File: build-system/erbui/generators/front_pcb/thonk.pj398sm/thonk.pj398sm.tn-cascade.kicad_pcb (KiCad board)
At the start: 2 copper layers, 4 parts, among them J1 IN

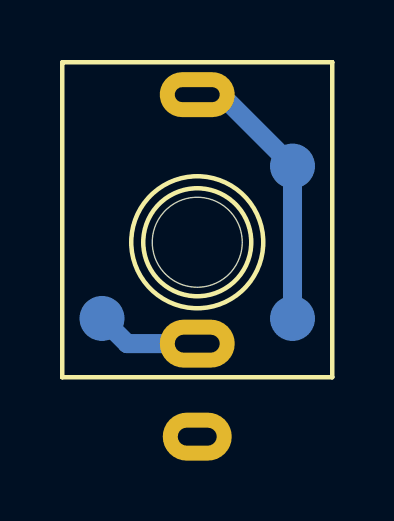
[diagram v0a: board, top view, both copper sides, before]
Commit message: Update thonk connector for cascade parts
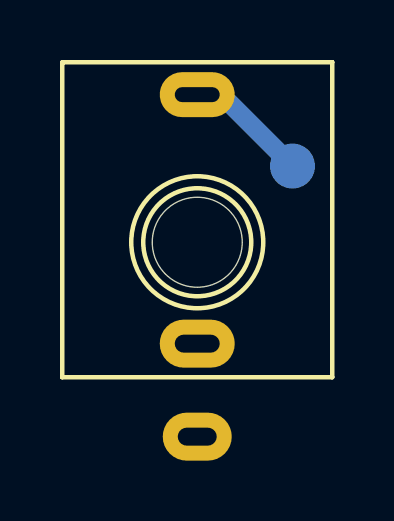
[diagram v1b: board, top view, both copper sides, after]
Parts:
- removed TP2, TP3: TestPoint, TestPoint:TestPoint_Pad_D1.5mm
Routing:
- net Net-(J1-PadT): track 9.24 -> 4.16 mm
- net Net-(J1-PadTN): track 3.52 -> 0.00 mm
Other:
- board text removed: "DI"
- board text removed: "DO"
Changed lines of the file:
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@@
   (general
     (thickness 1.6)
-    (drawings 3)
-    (tracks 5)
+    (drawings 1)
+    (tracks 2)
     (zones 0)
-    (modules 4)
+    (modules 2)
     (nets 4)
   )
@@
   )
   (setup
-    (last_trace_width 0.635)
+    (last_trace_width 0.1524)
     (user_trace_width 0.1524)
     (user_trace_width 0.254)
@@
       (effects (font (size 1 1) (thickness 0.15)))
     )
+    (fp_circle (center 0 0) (end 2.2 0) (layer F.SilkS) (width 0.15))
+    (fp_line (start -4.5 4.5) (end 4.5 4.5) (layer F.SilkS) (width 0.15))
+    (fp_line (start 4.5 -6) (end 4.5 4.5) (layer F.SilkS) (width 0.15))
+    (fp_line (start -4.5 -6) (end -4.5 4.5) (layer F.SilkS) (width 0.15))
+    (fp_line (start -4.5 -6) (end 4.5 -6) (layer F.SilkS) (width 0.15))
     (fp_circle (center 0 0) (end 1.8 0) (layer F.SilkS) (width 0.15))
-    (fp_line (start -4.5 -6) (end 4.5 -6) (layer F.SilkS) (width 0.15))
-    (fp_line (start -4.5 -6) (end -4.5 4.5) (layer F.SilkS) (width 0.15))
-    (fp_line (start 4.5 -6) (end 4.5 4.5) (layer F.SilkS) (width 0.15))
-    (fp_line (start -4.5 4.5) (end 4.5 4.5) (layer F.SilkS) (width 0.15))
-    (fp_circle (center 0 0) (end 2.2 0) (layer F.SilkS) (width 0.15))
     (pad "" np_thru_hole circle (at 0 0) (size 3 3) (drill 3) (layers *.Cu *.Mask))
     (pad T thru_hole oval (at 0 -4.92) (size 2.5 1.5) (drill oval 1.5 0.5) (layers *.Cu *.Mask)
@@
       (effects (font (size 1 1) (thickness 0.15)) (justify mirror))
     )
+    (fp_circle (center 0 0) (end 1.25 0) (layer B.CrtYd) (width 0.05))
     (fp_circle (center 0 0) (end 0 -0.95) (layer B.SilkS) (width 0.12))
-    (fp_circle (center 0 0) (end 1.25 0) (layer B.CrtYd) (width 0.05))
     (fp_text user %R (at 0 1.65) (layer B.Fab)
       (effects (font (size 1 1) (thickness 0.15)) (justify mirror))
@@
       (net 2 "Net-(J1-PadT)"))
   )
-  (module TestPoint:TestPoint_Pad_D1.5mm (layer B.Cu)
-    (at -3.175 2.54)
-    (descr "SMD pad as test Point, diameter 1.5mm")
-    (tags "test point SMD pad")
-    (attr virtual)
-    (fp_text reference TP3 (at 0 1.648) (layer B.SilkS) hide
-      (effects (font (size 1 1) (thickness 0.15)) (justify mirror))
-    )
-    (fp_text value TestPoint (at 0 -1.75) (layer B.Fab)
-      (effects (font (size 1 1) (thickness 0.15)) (justify mirror))
-    )
-    (fp_circle (center 0 0) (end 1.25 0) (layer B.CrtYd) (width 0.05))
-    (fp_circle (center 0 0) (end 0 -0.95) (layer B.SilkS) (width 0.12))
-    (fp_text user %R (at 0 1.65) (layer B.Fab)
-      (effects (font (size 1 1) (thickness 0.15)) (justify mirror))
-    )
-    (pad 1 smd circle (at 0 0) (size 1.5 1.5) (layers B.Cu B.Mask)
-      (net 1 "Net-(J1-PadTN)"))
-  )
-  (module TestPoint:TestPoint_Pad_D1.5mm (layer B.Cu)
-    (at 3.175 2.54)
-    (descr "SMD pad as test Point, diameter 1.5mm")
-    (tags "test point SMD pad")
-    (attr virtual)
-    (fp_text reference TP2 (at 0 1.648) (layer B.SilkS) hide
-      (effects (font (size 1 1) (thickness 0.15)) (justify mirror))
-    )
-    (fp_text value TestPoint (at 0 -1.75) (layer B.Fab)
-      (effects (font (size 1 1) (thickness 0.15)) (justify mirror))
-    )
-    (fp_circle (center 0 0) (end 0 -0.95) (layer B.SilkS) (width 0.12))
-    (fp_circle (center 0 0) (end 1.25 0) (layer B.CrtYd) (width 0.05))
-    (fp_text user %R (at 0 1.65) (layer B.Fab)
-      (effects (font (size 1 1) (thickness 0.15)) (justify mirror))
-    )
-    (pad 1 smd circle (at 0 0) (size 1.5 1.5) (layers B.Cu B.Mask)
-      (net 2 "Net-(J1-PadT)"))
-  )
-  (gr_text DO (at 3.175 0.635) (layer B.SilkS)
-    (effects (font (size 1 1) (thickness 0.15)) (justify mirror))
-  )
-  (gr_text DI (at -3.175 0.635) (layer B.SilkS)
-    (effects (font (size 1 1) (thickness 0.15)) (justify mirror))
-  )
   (gr_text pin (at 3.175 -4.445) (layer B.SilkS)
     (effects (font (size 1 1) (thickness 0.15)) (justify mirror))
   )
-  (segment (start -2.335 3.38) (end -3.175 2.54) (width 0.635) (layer B.Cu) (net 1))
-  (segment (start 0 3.38) (end -2.335 3.38) (width 0.635) (layer B.Cu) (net 1))
   (segment (start 0.795 -4.92) (end 3.175 -2.54) (width 0.635) (layer B.Cu) (net 2))
   (segment (start 0 -4.92) (end 0.795 -4.92) (width 0.635) (layer B.Cu) (net 2))
-  (segment (start 3.175 -2.54) (end 3.175 2.54) (width 0.635) (layer B.Cu) (net 2))
 )

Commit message: Optimize thonkiconn by reducing center hole and tightening pads
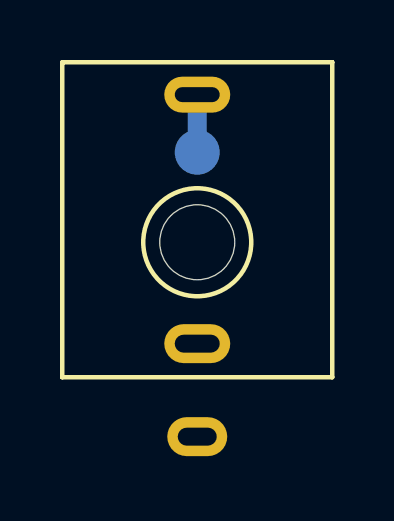
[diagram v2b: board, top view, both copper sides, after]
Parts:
- moved TP1 3.21 mm to (0.00, -3.00)
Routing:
- net Net-(J1-PadT): track 4.16 -> 1.92 mm
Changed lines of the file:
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@@
     (thickness 1.6)
     (drawings 1)
-    (tracks 2)
+    (tracks 1)
     (zones 0)
     (modules 2)
@@
     (mod_text_size 1 1)
     (mod_text_width 0.15)
-    (pad_size 2.3 1.6)
+    (pad_size 2 1.3)
     (pad_drill 1.3)
     (pad_to_mask_clearance 0.2)
@@
       (effects (font (size 1 1) (thickness 0.15)))
     )
-    (fp_circle (center 0 0) (end 2.2 0) (layer F.SilkS) (width 0.15))
     (fp_line (start -4.5 4.5) (end 4.5 4.5) (layer F.SilkS) (width 0.15))
     (fp_line (start 4.5 -6) (end 4.5 4.5) (layer F.SilkS) (width 0.15))
@@
     (fp_line (start -4.5 -6) (end 4.5 -6) (layer F.SilkS) (width 0.15))
     (fp_circle (center 0 0) (end 1.8 0) (layer F.SilkS) (width 0.15))
-    (pad "" np_thru_hole circle (at 0 0) (size 3 3) (drill 3) (layers *.Cu *.Mask))
-    (pad T thru_hole oval (at 0 -4.92) (size 2.5 1.5) (drill oval 1.5 0.5) (layers *.Cu *.Mask)
+    (pad "" np_thru_hole circle (at 0 0) (size 2.5 2.5) (drill 2.5) (layers *.Cu *.Mask))
+    (pad T thru_hole oval (at 0 -4.92) (size 2.2 1.2) (drill oval 1.5 0.5) (layers *.Cu *.Mask)
       (net 2 "Net-(J1-PadT)"))
-    (pad TN thru_hole oval (at 0 3.38) (size 2.5 1.6) (drill oval 1.5 0.6) (layers *.Cu *.Mask)
+    (pad TN thru_hole oval (at 0 3.38) (size 2.2 1.3) (drill oval 1.5 0.6) (layers *.Cu *.Mask)
       (net 1 "Net-(J1-PadTN)"))
-    (pad S thru_hole oval (at 0 6.48) (size 2.3 1.6) (drill oval 1.3 0.6) (layers *.Cu *.Mask)
+    (pad S thru_hole oval (at 0 6.48) (size 2 1.3) (drill oval 1.3 0.6) (layers *.Cu *.Mask)
       (net 3 GND))
   )
   (module TestPoint:TestPoint_Pad_D1.5mm (layer B.Cu)
-    (at 3.175 -2.54)
+    (at 0 -3)
     (descr "SMD pad as test Point, diameter 1.5mm")
     (tags "test point SMD pad")
@@
       (net 2 "Net-(J1-PadT)"))
   )
-  (gr_text pin (at 3.175 -4.445) (layer B.SilkS)
-    (effects (font (size 1 1) (thickness 0.15)) (justify mirror))
+  (gr_text pin (at -0.95 -3) (layer B.SilkS)
+    (effects (font (size 1 1) (thickness 0.15)) (justify left mirror))
   )
-  (segment (start 0.795 -4.92) (end 3.175 -2.54) (width 0.635) (layer B.Cu) (net 2))
-  (segment (start 0 -4.92) (end 0.795 -4.92) (width 0.635) (layer B.Cu) (net 2))
+  (segment (start 0 -4.92) (end 0 -3) (width 0.635) (layer B.Cu) (net 2))
 )

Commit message: Assign predictable pin names to controls
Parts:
- renumbered TP1 to Pin0, J1 to ZZ1
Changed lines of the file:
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@@
   )
   (net 0 "")
-  (net 1 "Net-(J1-PadTN)")
-  (net 2 "Net-(J1-PadT)")
-  (net 3 GND)
+  (net 1 GND)
+  (net 2 "Net-(Pin0-Pad1)")
+  (net 3 "Net-(Cascade0-Pad1)")
   (net_class Default "This is the default net class."
     (clearance 0.1524)
@@
     (diff_pair_gap 0.1524)
     (add_net GND)
-    (add_net "Net-(J1-PadT)")
-    (add_net "Net-(J1-PadTN)")
+    (add_net "Net-(Cascade0-Pad1)")
+    (add_net "Net-(Pin0-Pad1)")
   )
   (module Connector_Thonk:ThonkiconnJack (layer F.Cu)
     (at 0 0)
-    (fp_text reference J1 (at 0 -7.5) (layer F.SilkS) hide
+    (fp_text reference ZZ1 (at 0 -7.5) (layer F.SilkS) hide
       (effects (font (size 1 1) (thickness 0.15)))
     )
@@
     (pad "" np_thru_hole circle (at 0 0) (size 2.5 2.5) (drill 2.5) (layers *.Cu *.Mask))
     (pad T thru_hole oval (at 0 -4.92) (size 2.2 1.2) (drill oval 1.5 0.5) (layers *.Cu *.Mask)
-      (net 2 "Net-(J1-PadT)"))
+      (net 2 "Net-(Pin0-Pad1)"))
     (pad TN thru_hole oval (at 0 3.38) (size 2.2 1.3) (drill oval 1.5 0.6) (layers *.Cu *.Mask)
-      (net 1 "Net-(J1-PadTN)"))
+      (net 3 "Net-(Cascade0-Pad1)"))
     (pad S thru_hole oval (at 0 6.48) (size 2 1.3) (drill oval 1.3 0.6) (layers *.Cu *.Mask)
-      (net 3 GND))
+      (net 1 GND))
   )
   (module TestPoint:TestPoint_Pad_D1.5mm (layer B.Cu)
@@
     (tags "test point SMD pad")
     (attr virtual)
-    (fp_text reference TP1 (at 0 1.648) (layer F.SilkS) hide
+    (fp_text reference Pin0 (at 0 1.648) (layer F.SilkS) hide
       (effects (font (size 1 1) (thickness 0.15)))
     )
@@
     )
     (pad 1 smd circle (at 0 0) (size 1.5 1.5) (layers B.Cu B.Mask)
-      (net 2 "Net-(J1-PadT)"))
+      (net 2 "Net-(Pin0-Pad1)"))
   )
   (gr_text pin (at -0.95 -3) (layer B.SilkS)
